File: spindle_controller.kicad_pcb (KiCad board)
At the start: 2 copper layers, 62 x 124.5 mm, 70 parts, among them J1 VAC 230V, J2 AUX/CONTROL, J3 ICP, J4 Load output, J5 CONN_01X03, J6 CONN_01X03, J7 GND_JUMPER, J8 VCC_JUMPER, J9 Jack_3.5mm_4pin, Q1 2N3904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

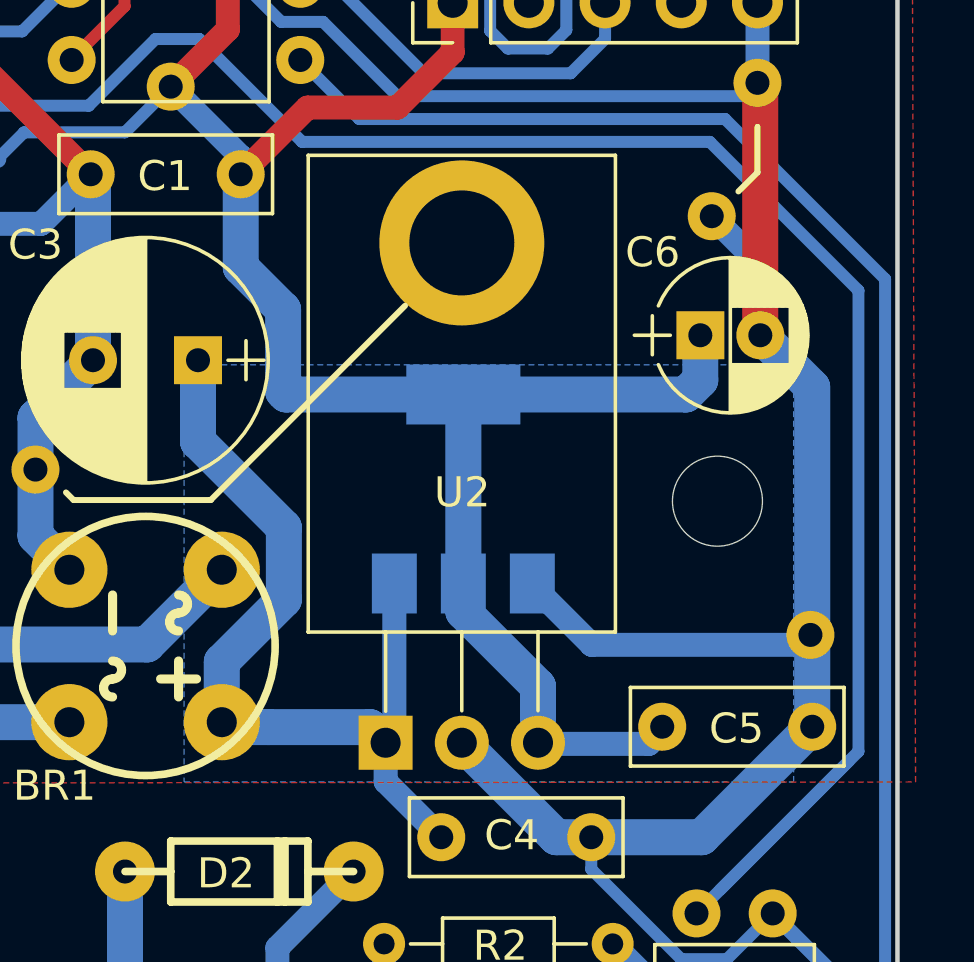
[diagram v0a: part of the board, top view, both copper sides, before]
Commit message: Small updates to VCC plane at 1117 regulator.
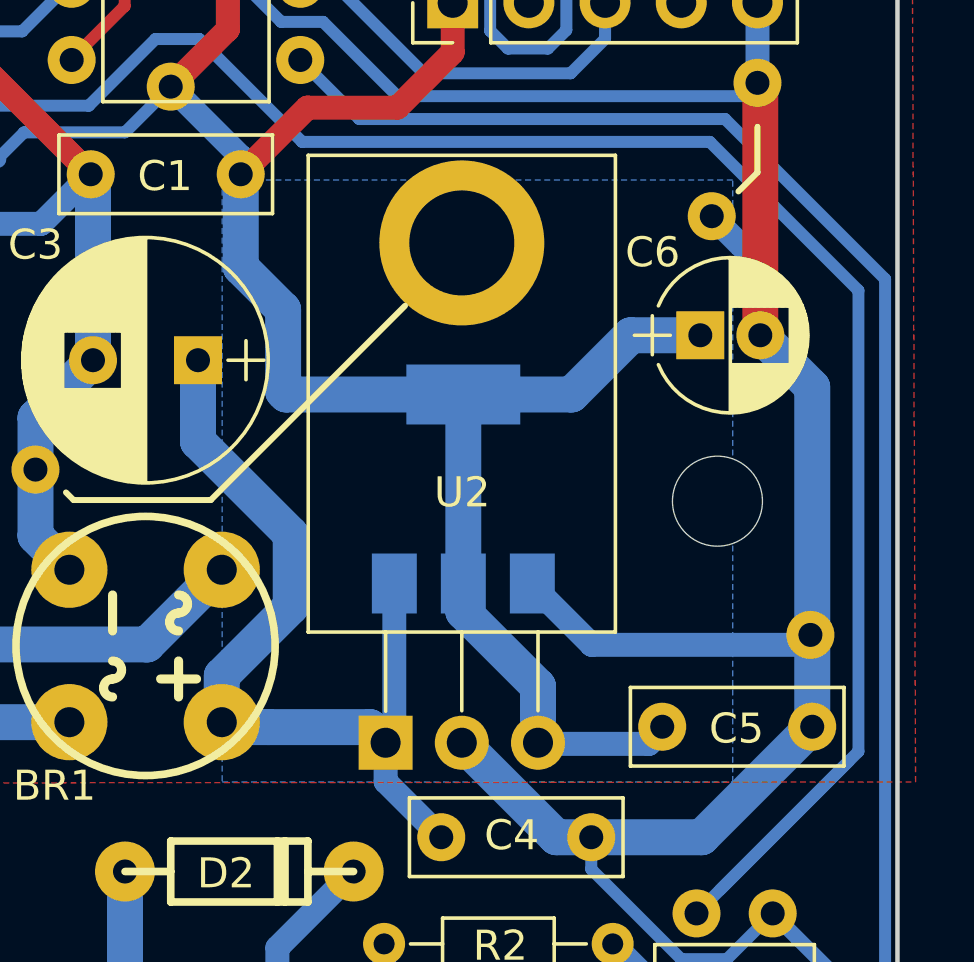
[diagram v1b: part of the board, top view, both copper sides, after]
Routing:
- net VCC: track 241.1 -> 240.2 mm
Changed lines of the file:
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@@
-(kicad_pcb (version 20170123) (host pcbnew "(2017-03-10 revision de30dc9f5)-makepkg")
+(kicad_pcb (version 20170123) (host pcbnew "(2017-05-14 revision 14bb238b3)-makepkg")
   (general
     (links 142)
-    (no_connects 2)
+    (no_connects 1)
     (area 30.407667 34.864999 126.891001 166.69)
     (thickness 1.6)
@@
   )
   (setup
-    (last_trace_width 0.4)
+    (last_trace_width 0.25)
     (user_trace_width 0.25)
     (user_trace_width 0.4)
@@
     (visible_elements 7FFFEF7F)
     (pcbplotparams
-      (layerselection 0x00030_ffffffff)
-      (usegerberextensions false)
+      (layerselection 0x010f0_ffffffff)
+      (usegerberextensions true)
       (excludeedgelayer true)
       (linewidth 0.100000)
@@
       (viasonmask false)
       (mode 1)
-      (useauxorigin false)
+      (useauxorigin true)
       (hpglpennumber 1)
       (hpglpenspeed 20)
@@
       (outputformat 1)
       (mirror false)
-      (drillshape 1)
+      (drillshape 0)
       (scaleselection 1)
-      (outputdirectory ""))
+      (outputdirectory Production))
   )
   (net 0 "")
@@
   (segment (start 117.2845 130.8735) (end 117.2845 126.4285) (width 0.5) (layer B.Cu) (net 12) (status 30))
   (segment (start 117.2845 126.4285) (end 117.1575 126.3015) (width 0.5) (layer B.Cu) (net 12) (status 30))
+  (segment (start 106.8451 101.3837) (end 110.4523 101.3837) (width 1.2) (layer B.Cu) (net 13))
+  (segment (start 110.4523 101.3837) (end 112.4265 99.4095) (width 1.2) (layer B.Cu) (net 13))
+  (segment (start 112.4265 99.4095) (end 114.7445 99.4095) (width 1.2) (layer B.Cu) (net 13))
   (segment (start 111.3155 60.3885) (end 114.3 63.373) (width 0.4) (layer B.Cu) (net 13))
   (segment (start 114.3 63.373) (end 114.3 75.184) (width 0.4) (layer B.Cu) (net 13))
@@
   (segment (start 100.838 101.2825) (end 100.9392 101.3837) (width 1.2) (layer B.Cu) (net 13))
   (segment (start 100.9392 101.3837) (end 106.8451 101.3837) (width 1.2) (layer B.Cu) (net 13))
-  (segment (start 106.8451 101.3837) (end 114.2623 101.3837) (width 1.2) (layer B.Cu) (net 13))
-  (segment (start 114.2623 101.3837) (end 114.7445 100.9015) (width 1.2) (layer B.Cu) (net 13))
-  (segment (start 114.7445 100.9015) (end 114.7445 99.4095) (width 1.2) (layer B.Cu) (net 13))
   (segment (start 109.3343 112.9919) (end 109.3724 113.03) (width 0.8) (layer B.Cu) (net 13))
   (segment (start 109.3724 113.03) (end 113.03 113.03) (width 0.8) (layer B.Cu) (net 13))
@@
   (segment (start 100.1395 134.5565) (end 100.1395 131.5085) (width 0.8) (layer B.Cu) (net 40))
   (segment (start 100.1395 131.5085) (end 103.1875 128.4605) (width 0.8) (layer B.Cu) (net 40) (status 20))
-  (segment (start 98.7933 112.3061) (end 98.7933 110.289702) (width 1.2) (layer B.Cu) (net 41))
-  (segment (start 98.7933 110.289702) (end 100.863301 108.219701) (width 1.2) (layer B.Cu) (net 41))
-  (segment (start 100.863301 108.219701) (end 100.863301 105.816301) (width 1.2) (layer B.Cu) (net 41))
-  (segment (start 100.863301 105.816301) (end 98.0007 102.9537) (width 1.2) (layer B.Cu) (net 41))
+  (segment (start 98.7933 112.3061) (end 98.7933 110.7567) (width 1.2) (layer B.Cu) (net 41))
+  (segment (start 98.7933 110.7567) (end 101.092 108.458) (width 1.2) (layer B.Cu) (net 41))
+  (segment (start 101.092 108.458) (end 101.092 106.045) (width 1.2) (layer B.Cu) (net 41))
+  (segment (start 101.092 106.045) (end 98.0007 102.9537) (width 1.2) (layer B.Cu) (net 41))
   (segment (start 98.0007 102.9537) (end 98.0007 100.2411) (width 1.2) (layer B.Cu) (net 41))
   (segment (start 103.7336 112.4712) (end 100.3554 112.4712) (width 1.2) (layer B.Cu) (net 41))
@@
     (polygon
       (pts
-        (xy 97.536 100.3935) (xy 97.536 114.3) (xy 117.856 114.3) (xy 117.856 100.3935)
+        (xy 98.806 94.234) (xy 98.806 114.3) (xy 115.824 114.3) (xy 115.824 94.234)
       )
     )
